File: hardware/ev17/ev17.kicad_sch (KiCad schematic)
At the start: 180 parts, among them CN1 Conn_05x02_Female, CN2 PJ-242, J1 USB_C_Receptacle, J11 Conn_02x05_Counter_Clockwise, J12 Conn_01x01, J13 Conn_01x01, J14 Conn_01x01, J15 Conn_01x01, J16 Conn_01x01, J17 Conn_01x01, J18 Conn_01x01, J19 Conn_01x01, J2 Conn_01x02_Socket, J20 Conn_01x01, J21 Conn_01x01, J3 AudioJack4, J4 Conn_02x03_Odd_Even, J5 Conn_02x03_Odd_Even, J6 Conn_02x05_Counter_Clockwise, J7 Conn_02x05_Counter_Clockwise, J8 Conn_02x05_Counter_Clockwise, J9 Conn_02x05_Counter_Clockwise, Q1 2N7002, Q2 2N7002, Q3 2N7002, SW1 SW_SPDT, SW2 SW_Push, SW3 SW_Push, SW4 SW_Push, SW5 SW_Push, SW6 SW_Push, SW7 SW_Push, U1 BQ21040DBV, U10 STM32F405RGTx, U12 XC6227C301MR-G, U2 USBLC6-2P6, U3 STM32F072CBTx, U4 CH340C, U5 TPS63060, U6 WM8960CGEFL/RV, U7 ESP32-S3-WROOM-1, U8 M24C02-RMN6TP, U9 TPS2116DRL, Y1 Crystal_GND24

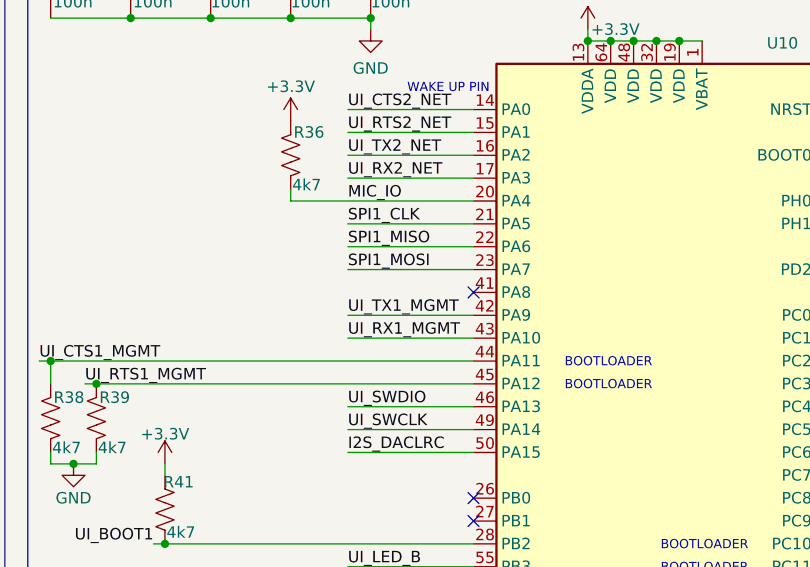
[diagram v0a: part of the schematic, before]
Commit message: Moved esp32s3 8mm down. Adjusted pins to final layout, ever touch again, please! Moved leds to the top right. (refs #402, #423, #404)
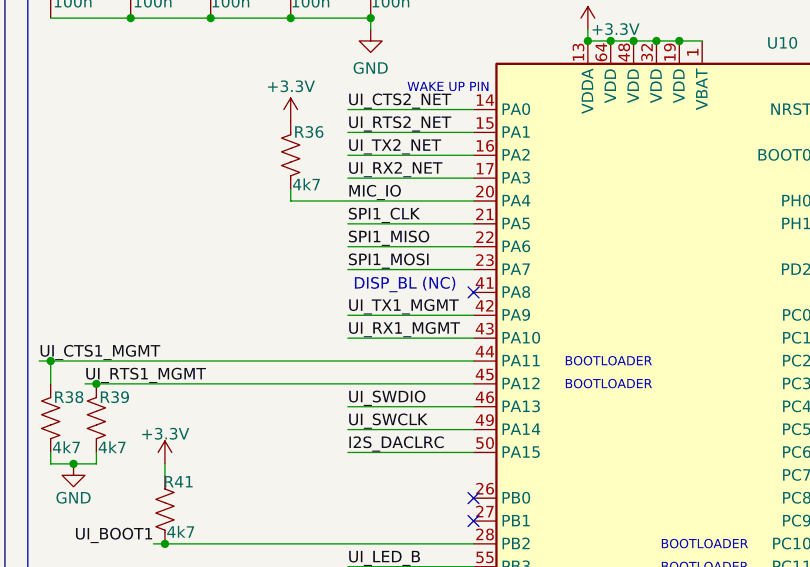
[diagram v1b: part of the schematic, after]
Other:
- note added: "DISP_BL (NC)"
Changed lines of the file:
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@@
+		)
+	)
+	(text "DISP_BL (NC)"
+		(exclude_from_sim no)
+		(at 422.91 83.058 0)
+		(effects
+			(font
+				(size 1.27 1.27)
+			)
 		)
 	)

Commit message: Updated ptt buttons to longer stem version (refs #424)
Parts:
- SW4, SW5: JLCPCB Part # C318884 -> C318886
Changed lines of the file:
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@@
 			)
 		)
-		(property "JLCPCB Part #" "C318884"
+		(property "JLCPCB Part #" "C318886"
 			(at 532.638 108.204 0)
 			(effects
@@
 			)
 		)
-		(property "JLCPCB Part #" "C318884"
+		(property "JLCPCB Part #" "C318886"
 			(at 532.638 77.724 0)
 			(effects

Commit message: Added current sense resistors for each chip and put them on an external connector. (refs #417)
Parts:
- removed J12, J13, J14, J15, J16, J20, J21: Conn_01x01, Connector_PinSocket_2.00mm:PinSocket_1x01_P2.00mm_Vertical, symbol Connector_Generic:Conn_01x01
- added J10: Conn_02x05_Counter_Clockwise, Hactar_Footprints:HDR-SMD_10P-P2.54-V-F-R2-C5-LS7.1-1, symbol Connector_Generic:Conn_02x05_Counter_Clockwise
- added R63, R76, R77, R78, R79, R80: 0R1, Resistor_SMD:R_0603_1608Metric, symbol Device:R_US
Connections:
- net +3.3V: now also R63.2, R76.2, R77.2, R78.2, R79.2, R80.2; no longer NT2.2, U10.1 (VBAT), U10.13 (VDDA), U10.19 (VDD), U10.32 (VDD), U10.48 (VDD), U10.64 (VDD), U3.1 (VBAT), U3.24 (VDD), U3.36 (VDDIO2), U3.48 (VDD), U3.9 (VDDA), U4.16 (VCC), U6.10 (DBVDD), U6.8 (DCVDD), U7.2 (3V3), U8.8 (VCC)
- net VSYS: now also J10.1 (Pin_1)
- net BB_Vout_Sense: now reaches C22.1, C24.1, C27.1, C29.1, C30.1, C31.1, C35.1, R26.2, R28.2, R48.1, U5.9 (VOUT)
- net BB_Vout_Sense: now also J10.3 (Pin_3)
- net Analog_Sense: now reaches C10.1, C18.1, R52.1, U12.5 (VOUT)
- net Analog_Sense: now also J10.4 (Pin_4)
- net BB_Vin_Sense: now reaches C14.1, C15.1, C16.1, R14.2, R18.1, U5.2 (VIN)
- net BB_Vin_Sense: now also J10.2 (Pin_2)
- new net CH340C_Sense: J10.5 (Pin_5), NT2.2, R80.1, U4.16 (VCC)
- new net EEPROM_Sense: J10.9 (Pin_9), R79.1, U8.8 (VCC)
- new net MGMT_Sense: J10.8 (Pin_8), R77.1, U3.1 (VBAT), U3.24 (VDD), U3.36 (VDDIO2), U3.48 (VDD), U3.9 (VDDA)
- new net NET_Sense: J10.6 (Pin_6), R76.1, U7.2 (3V3)
- new net UI_Sense: J10.7 (Pin_7), R78.1, U10.1 (VBAT), U10.13 (VDDA), U10.19 (VDD), U10.32 (VDD), U10.48 (VDD), U10.64 (VDD)
- new net WM8960_Sense: J10.10 (Pin_10), R63.1, U6.10 (DBVDD), U6.8 (DCVDD)
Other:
- note added: "Current Sense Connector"
- moved on the sheet: C13, C21, C23, C25, C26, C28, C32, C33, C34, C36, C37, C48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

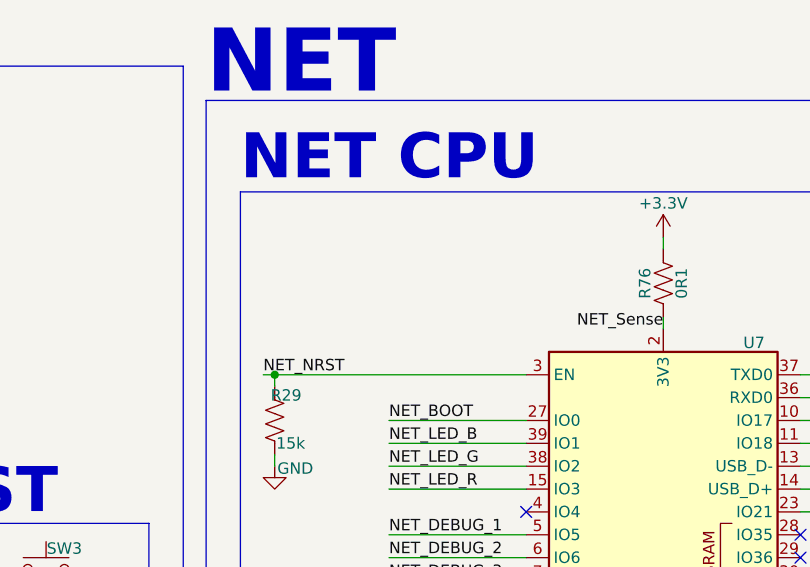
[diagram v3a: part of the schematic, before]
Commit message: Added caps near esp32s3 power pins (refs #405)
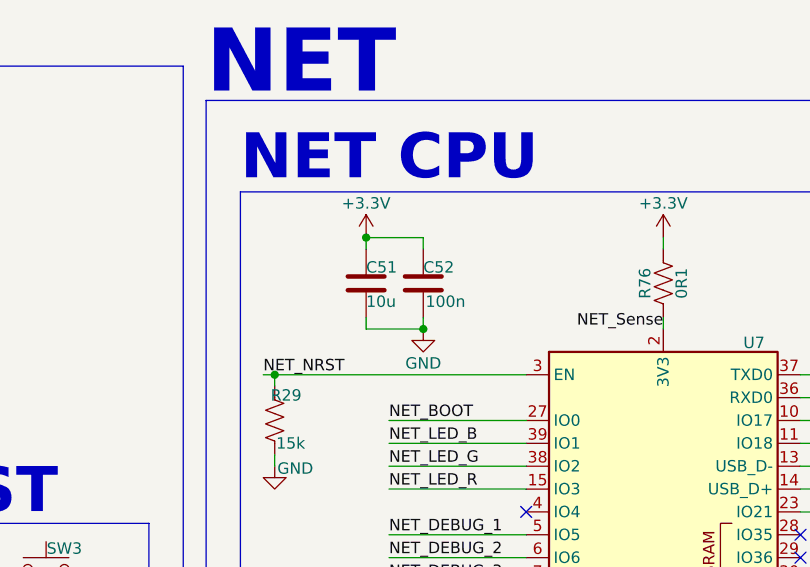
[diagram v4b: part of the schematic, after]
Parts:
- added C51: 10u, Capacitor_SMD:C_0805_2012Metric, symbol Device:C
- added C52: 100n, Capacitor_SMD:C_0402_1005Metric, symbol Device:C
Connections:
- net +3.3V: now also C51.1, C52.1
- net GND: now also C51.2, C52.2

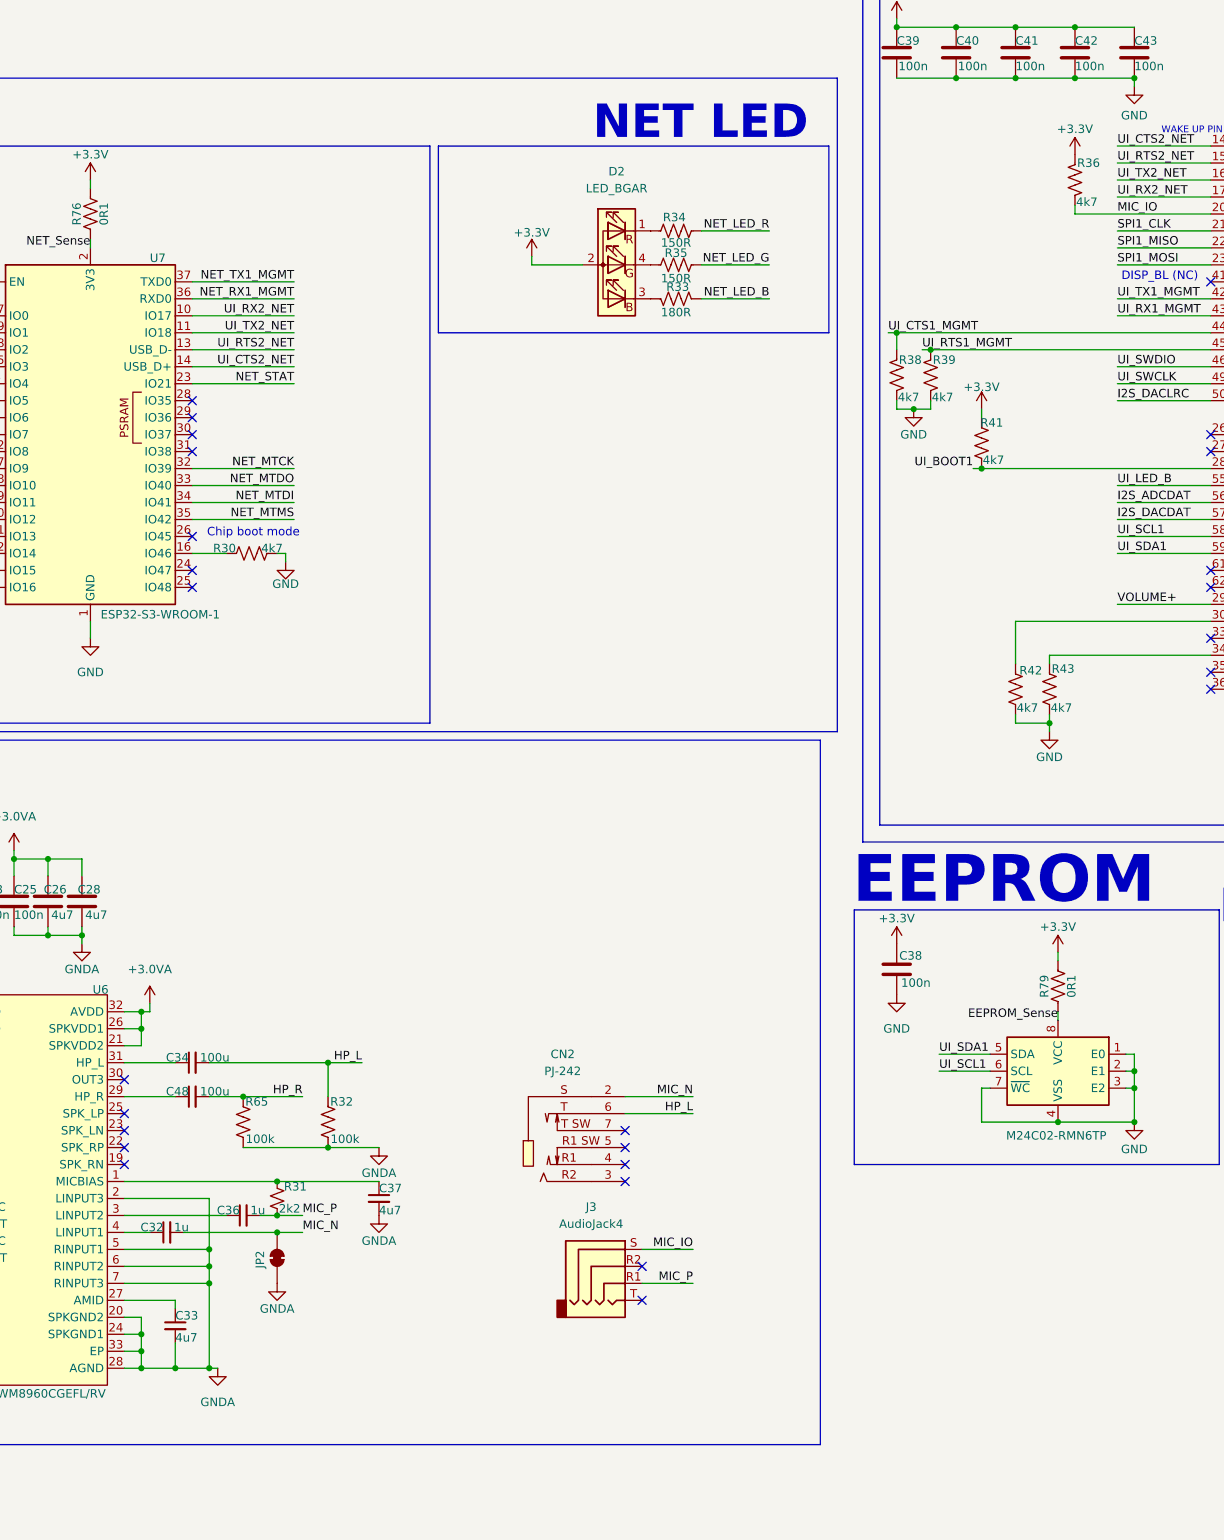
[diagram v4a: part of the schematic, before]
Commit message: Added RC circuit for mic line with approximately 47ms rise and fall times. (refs #408, #429)
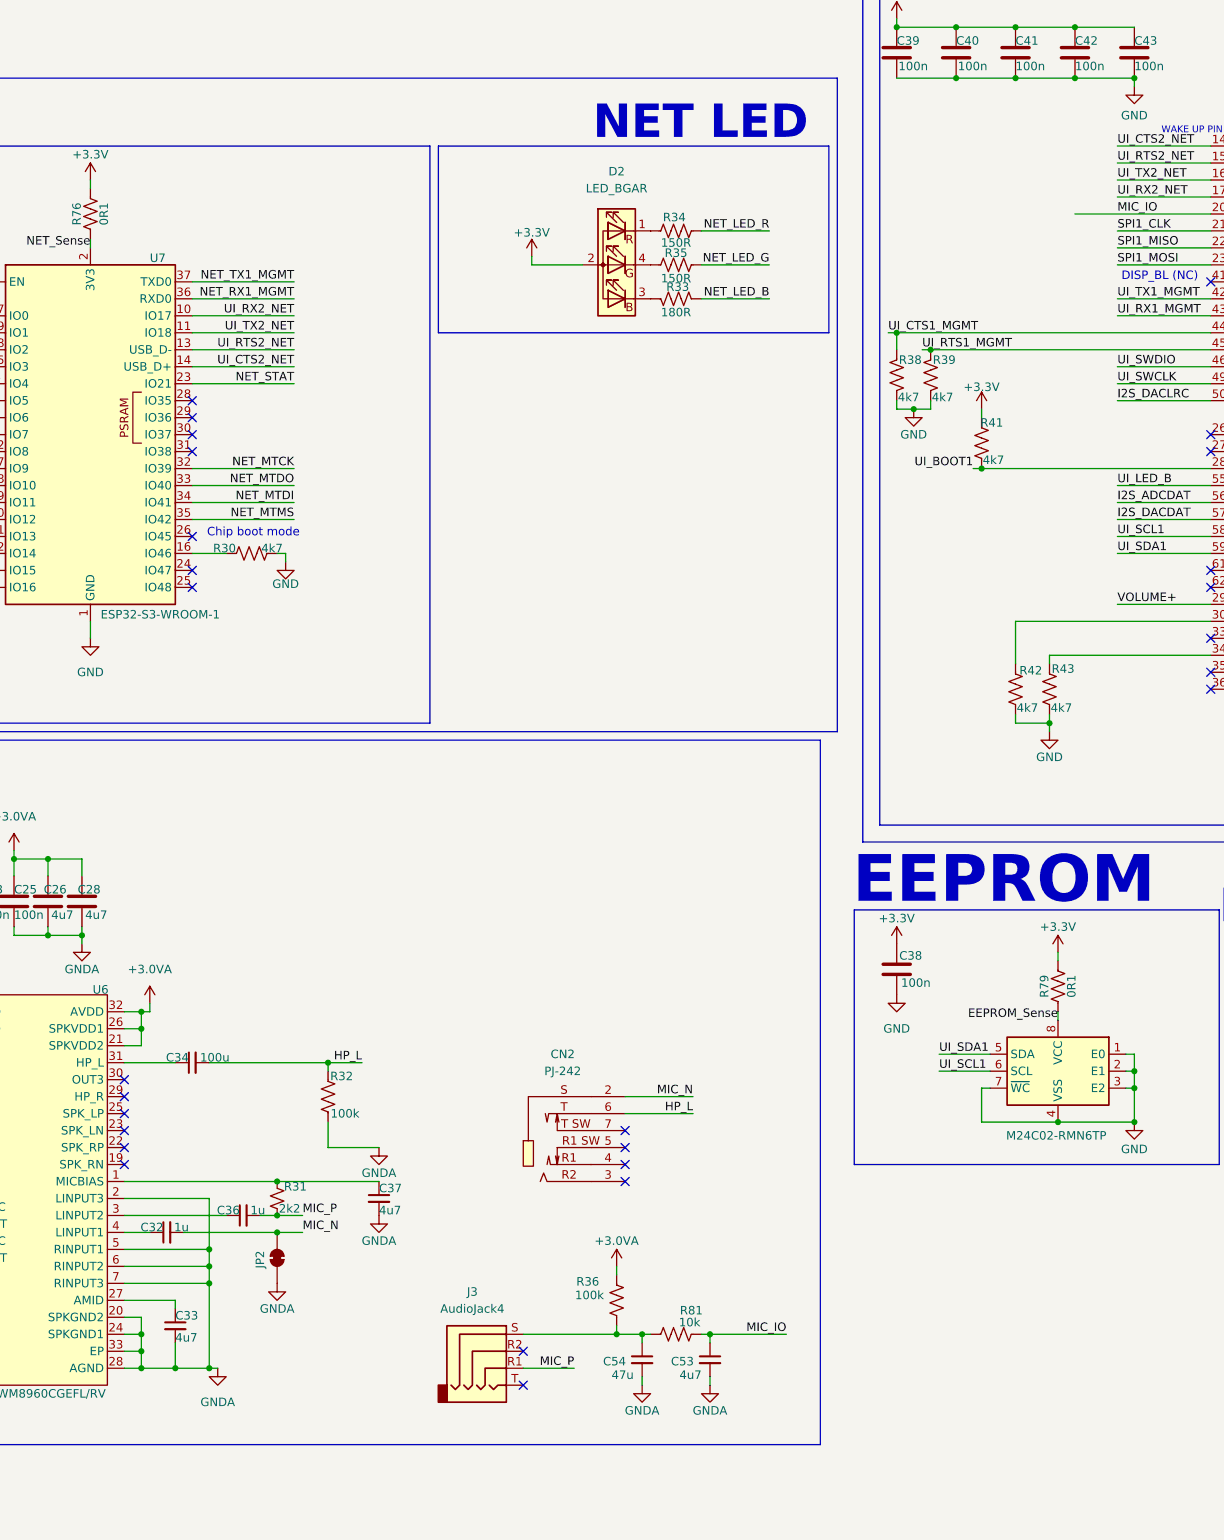
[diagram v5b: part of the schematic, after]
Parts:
- removed C48: 100u, Capacitor_SMD:C_1206_3216Metric, symbol Device:C_Small
- removed R65: 100k, Resistor_SMD:R_0402_1005Metric, symbol Device:R_US
- added C53: 4u7, Capacitor_SMD:C_0402_1005Metric, symbol Device:C_Small
- added C54: 47u, Capacitor_SMD:C_0805_2012Metric, symbol Device:C_Small
- added R81: 10k, Resistor_SMD:R_0402_1005Metric, symbol Device:R_US
- R36: value 4k7 -> 100k; JLCPCB Part # C25900 -> C25741
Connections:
- net +3.0VA: now also R36.2
- net +3.3V: no longer R36.2
- net GNDA: now also C53.2, C54.2
- net MIC_IO: now also C53.1, R81.2; no longer J3.S, R36.1
- new net: C54.1, J3.S, R36.1, R81.1
- no-connect marks 58 -> 59
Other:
- moved on the sheet: J3, R32
